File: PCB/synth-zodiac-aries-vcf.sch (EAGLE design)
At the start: 75 parts, among them J4 6.35MM JACK, Q2 PMP4201, Q3 PMP4201, Q4 PMP4201, Q5 PMP4201, Q6 PMP4201, Q7 BC847BPN, Q8 PNP, U2 LM13700, U6 NE5532A

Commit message: Snapshot of designs so far.
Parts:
- removed AUD_OUT, TP1, TP17: TPTHD-038, con-testpoints:TPTHD-038
- removed C22, C23, C24, C25, C27, C29, C30, C34, C35: 0.1uF, rlc:CAPACITOR0603
- removed C26: 100uF/25V, rlc:CAPACITOR_POL-ALUM-SMT-6.3
- removed C28, C31, C32: 2.2uF, rlc:CAPACITOR0603
- removed C33: 2.2uF/16V, rlc:CAPACITOR_POL-ALUM-SMT-4
- removed GND_VCA: TPTHD-SCOPE-LOOP, con-testpoints:TPTHD-SCOPE-LOOP
- removed J4: 6.35MM JACK, con-trs:TRS-JACK-STEREOTE-CK-6.35-29B
- removed JMP1, JMP3, JMP4, JMP5, JMP6, JMP7: NP, rlc:RESISTOR0603
- removed JMP57, JMP58, JMP62: 0, rlc:RESISTOR0603
- removed Q8: PNP, transistor-bjt:PNP-BC856
- removed R26, R29, R32, R34: 1.0K, rlc:RESISTOR0603
- removed R30, R31: 2.74K, rlc:RESISTOR0603
- removed R33, R44, R51: 12.1K, rlc:RESISTOR0603
- removed R35, R41: 68.1K, rlc:RESISTOR0603
- removed R36, R47: 33.2K, rlc:RESISTOR0603
- removed R37: 100K, rlc:RESISTOR0603
- removed R38: 47.5K, rlc:RESISTOR0603
- removed R39, R40, R49: 4.99K, rlc:RESISTOR0603
- removed R42: 100, rlc:RESISTOR0603
- removed R43: 6.81K, rlc:RESISTOR0603
- removed R46, R48: 681R, rlc:RESISTOR0603
- removed R50, R54, R55: 10.0K, rlc:RESISTOR0603
- removed R52: 475R, rlc:RESISTOR0603
- removed R53: 4.75M, rlc:RESISTOR0603
- removed R56: 499K, rlc:RESISTOR0603
- removed U2: LM13700, op-amp:DUAL-BIASLM13700-SMD
- removed VR3, VR4: 10K, rlc:POTRK09?113
- removed VR7: 10K, rlc:TRIMPOTTC33X
- added C1, C8, C9: 2.2uF, rlc:CAPACITOR0603
- added C10, C11, C2, C3, C4, C5, C7: 0.1uF, rlc:CAPACITOR0603
- added C6: 100uF/25V, rlc:CAPACITOR_POL-ALUM-SMT-6.3
- added CAL: 10K, rlc:TRIMPOTTC33X
- added CONST: Aries, circuit-monkey-zodiac:CONSTELLATION-ARIES
- added CUTOFF, RES: 10K, rlc:TRIMPOT9MM_PCB_SHAFT
- added CV_VCF, CV_VCF_MOD, MOD_MIX, TP_VCF_OUT: TPSMD-040-RND, con-testpoints:TPSMD-040-RND
- added GLYPH: Aries, circuit-monkey-zodiac:GLYPH-ARIES
- added J1: (no value), con-jst:04P-VT-SMT
- added MOD_IN, VCF_MOD: 2-pin, VT, SMT, con-jst:02PVT-SMT
- added PCB: PCB FAB, circuit-monkey-zodiac:PENTAGON-40R
- added R1, R7: 68.1K, rlc:RESISTOR0603
- added R10, R11, R12, R13, R15, R16, R18, R8: 1.0K, rlc:RESISTOR0603
- added R14, R9: 2.74K, rlc:RESISTOR0603
- added R17: 12.1K, rlc:RESISTOR0603
- added R2: 47.5K, rlc:RESISTOR0603
- added R4: 33.2K, rlc:RESISTOR0603
- added R5, R6: 4.99K, rlc:RESISTOR0603
- added SHORT1: NP, rlc:SHORT0603
- JMP2: value NP -> 0
- R19: value 100K -> 100
- R20: value 1.0K -> 6.81K
- R21: value 1.0K -> 12.1K
- R22, R3: value 1.0K -> 100K
- VCF_OUT: value TPTHD-038 -> 2-pin, VT, SMT; device con-testpoints:TPTHD-038 -> con-jst:02PVT-SMT
- renumbered R45 to R19
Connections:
- removed net AUDIO_OUT: AUD_OUT.P$1, J4.T, R52.2
- removed net EXP_VCA_CV: R55.1, R56.2
- removed net N$44: C28.2, Q6-A.BASE, R3.2
- removed net N$45: R46.2, U2-B.-
- removed net N$50: Q7P.BASE, R34.2, R35.2, R36.2, R37.2, R38.2, TP17.P$1
- removed net N$51: R35.1, VR7.2
- removed net N$54: R37.1, VR3POT.2
- removed net N$60: R47.2, R48.2, U2-B.+
- removed net N$61: TP1.P$1, U2-B.DIODE-BIAS
- removed net N$62: R49.2, U2-B-BUFFER.IN, U2-B.OUT
- removed net N$63: R50.2, U2-B.AMP-BIAS
- removed net N$64: C33.P, R51.2, U2-B-BUFFER.OUT
- removed net N$65: C33.N, R52.1
- removed net N$66: Q8.COLLECTOR, R50.1, R53.2
- removed net N$67: JMP62.2, Q8.EMITTER
- removed net N$68: JMP62.1, R54.2, R55.2
- removed net N$69: JMP1.2, U2-A.-
- removed net N$70: JMP3.2, U2-A.+
- removed net N$71: JMP5.1, U2-A.OUT
- removed net N$72: JMP2.2, U2-A.DIODE-BIAS
- removed net N$73: JMP4.2, U2-A.AMP-BIAS
- removed net N$74: JMP6.2, U2-A-BUFFER.IN
- removed net N$75: JMP7.1, U2-A-BUFFER.OUT
- removed net VCA_CV: R54.1
- new net CAL: CAL.2, R7.1
- new net CUTOFF: CUTOFF.2, R3.1
- new net MOD_MIX: MOD_MIX.P$1, Q7P.BASE, R2.2, R3.2, R4.2, R7.2, R8.2
- new net VCO_MIX: C1.2, Q6-A.BASE, R15.2
- net +9V: now also C10.2, CUTOFF.3, J1.1, R17.2, R9.2, U6-PWR.V+; no longer C29.2, C34.2, R30.2, R33.2, U2-PWR.VDD, U6-PWR.VDD, VR3POT.3
- net -9V: now also C11.1, CUTOFF.1, J1.2, R6.1, U6-PWR.V-; no longer C30.1, C35.1, R39.1, R53.1, R56.1, U2-PWR.GND, U6-PWR.GND, VR3POT.1
- net EXP_VCF_CV: now also CV_VCF_MOD.P$1, R2.1; no longer R38.1
- net FILT(+): now also C2.2; no longer C22.2
- net FILT(-): now also C2.1; no longer C22.1
- net GND: now also C10.1, C11.2, C6.N, C7.2, J1.4, MOD_IN.2, PCB.GND@1, R14.1, R22.1, R5.2, R8.1, RES.1, VCF_MOD.2, VCF_OUT.2; no longer C26.N, C27.2, C29.1, C30.2, C34.1, C35.2, GND_VCA.P$1, J4.S, Q8.BASE, R19.1, R31.1, R34.1, R40.2, R46.1, R48.1, R49.1, R51.1, VR3-MNT.GND@MT1, VR3-MNT.GND@MT2, VR4-MNT.GND@MT1, VR4-MNT.GND@MT2, VR4POT.1
- net N$32: now also R19.2, R20.1; no longer R42.2, R43.1
- net N$33: now also C8.2, JMP2.1, R22.2; no longer C31.2, JMP58.1, R19.2
- net N$34: now also R10.2, R9.1; no longer R21.2, R30.1
- net N$35: now also C3.1; no longer C23.1
- net N$36: now also C3.2; no longer C23.2
- net N$37: now also R10.1, R11.2; no longer R21.1, R22.2
- net N$38: now also C4.1; no longer C24.1
- net N$39: now also C4.2; no longer C24.2
- net N$40: now also R11.1, R12.2; no longer R22.1, R26.2
- net N$41: now also C5.1; no longer C25.1
- net N$42: now also C5.2; no longer C25.2
- net N$43: now also R12.1, R13.2; no longer R26.1, R29.2
- net N$46: now also R18.2; no longer R32.2
- net N$47: now also R18.1; no longer R32.1
- net N$48: now also C6.P, R13.1, R14.2, R15.1, R16.1; no longer C26.P, R20.1, R29.1, R3.1, R31.2
- net N$49: now also C7.1, R17.1; no longer C27.1, R33.1
- net N$52: now also CAL.3, R6.2; no longer R39.2, VR7.3
- net N$53: now also CAL.1, R5.1; no longer R40.1, VR7.1
- net N$55: now also C1.1, R1.2; no longer C28.1, R41.2
- net N$56: now also R19.1; no longer R42.1
- net N$57: now also C8.1, R20.2, R21.2; no longer C31.1, R43.2, R44.2
- net N$58: now also R21.1, RES.3; no longer R44.1, VR4POT.3
- net N$59: now also C9.2, RES.2; no longer C32.2, VR4POT.2
- net RES_INPUT: now also C9.1, R16.2; no longer C32.1, R20.2
- net VCF_IN: now also CV_VCF.P$1, R1.1, SHORT1.2; no longer JMP57.2, R41.1
- net VCF_MOD: now also R4.1, VCF_MOD.1; no longer R36.1
- net VCF_OUT: now also JMP2.2, TP_VCF_OUT.P$1, VCF_OUT.1; no longer JMP58.2, R47.1, VCF_OUT.P$1
- net VCO_OUT: now also MOD_IN.1, SHORT1.1; no longer JMP57.1
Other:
- note added: "2.6V"
- note added: "3.55V"
- note added: "4.5V"
- note added: "5.45V"
- note added: "6.4V"
- note added: "===> VCA"
- note added: "CV Panel ===>"
- note added: "NC"
- note added: "VCF MOD ===>"
- note added: "VCO / CV Panel ===>"
- note removed: "10.6V"
- note removed: "4.3V"
- note removed: "5.8V"
- note removed: "7.4V"
- note removed: "9.4V"
- note removed: "VCA"
- moved on the sheet: JMP2, Q2-A, Q2-B, Q3-A, Q3-B, Q4-A, Q4-B, Q5-A, Q5-B, Q6-A, Q6-B, Q7N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

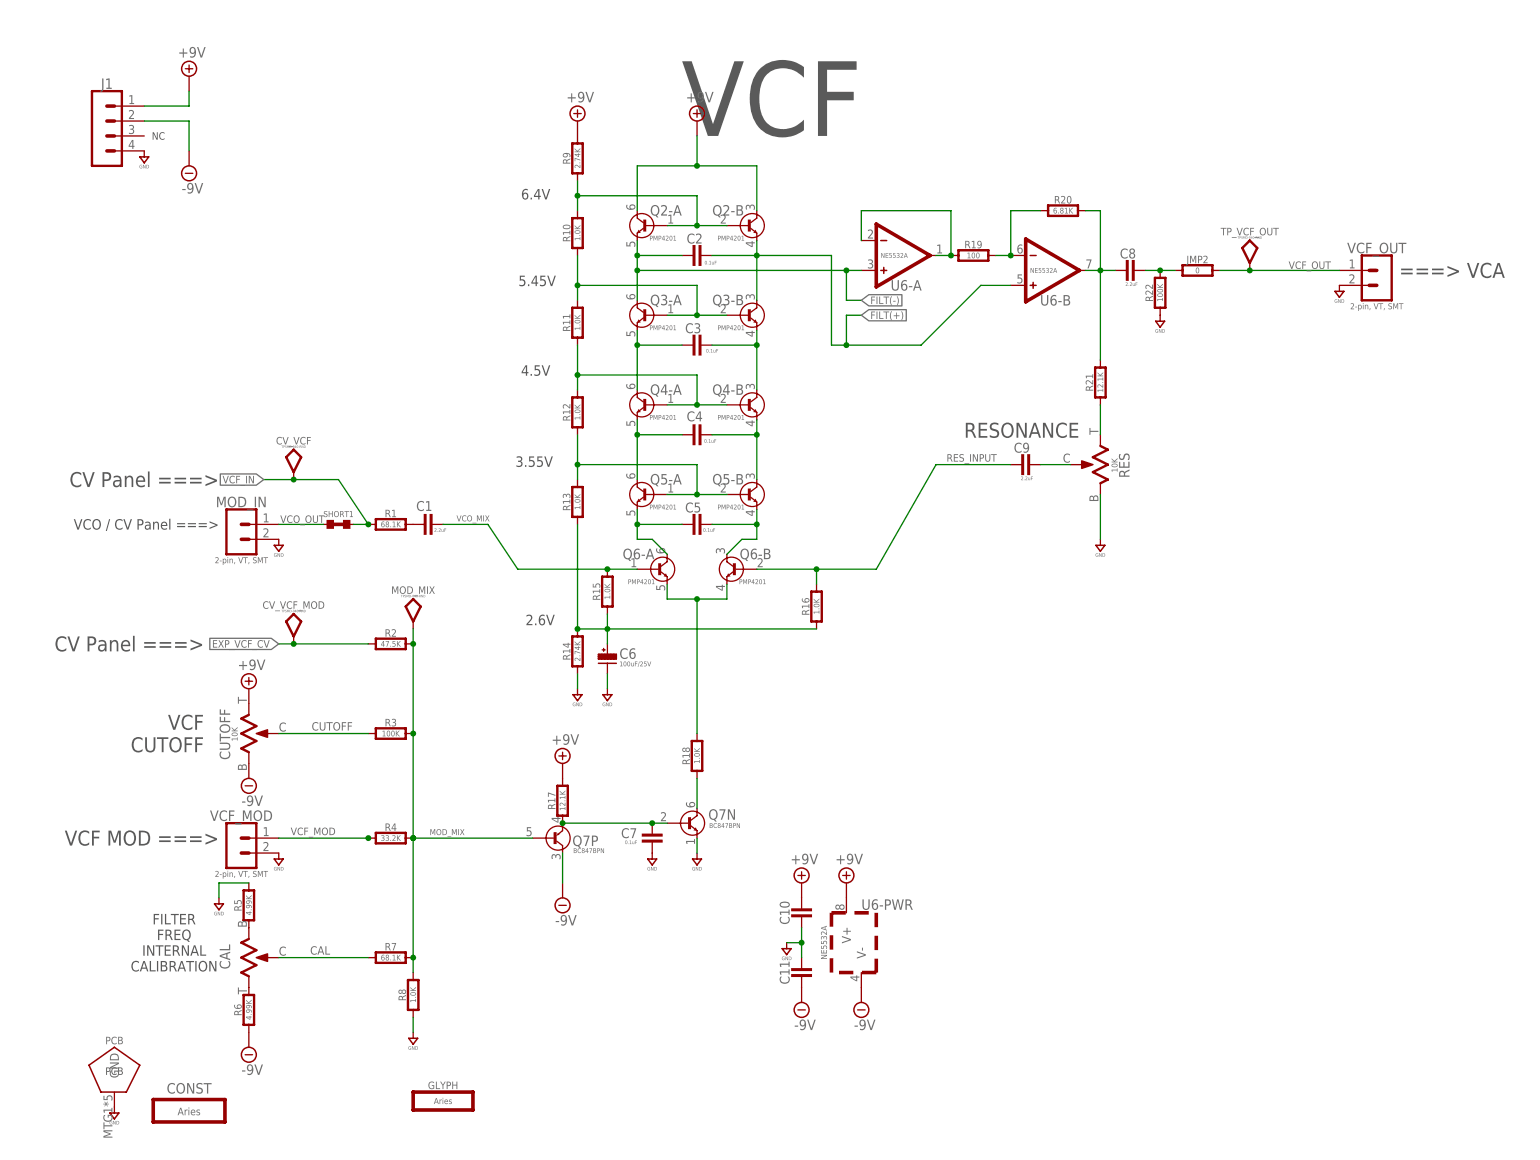
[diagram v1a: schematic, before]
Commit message: Almost ready for FAB.
Sagittarius was mis-spelled, renamed it.  Taurus is still WIP.
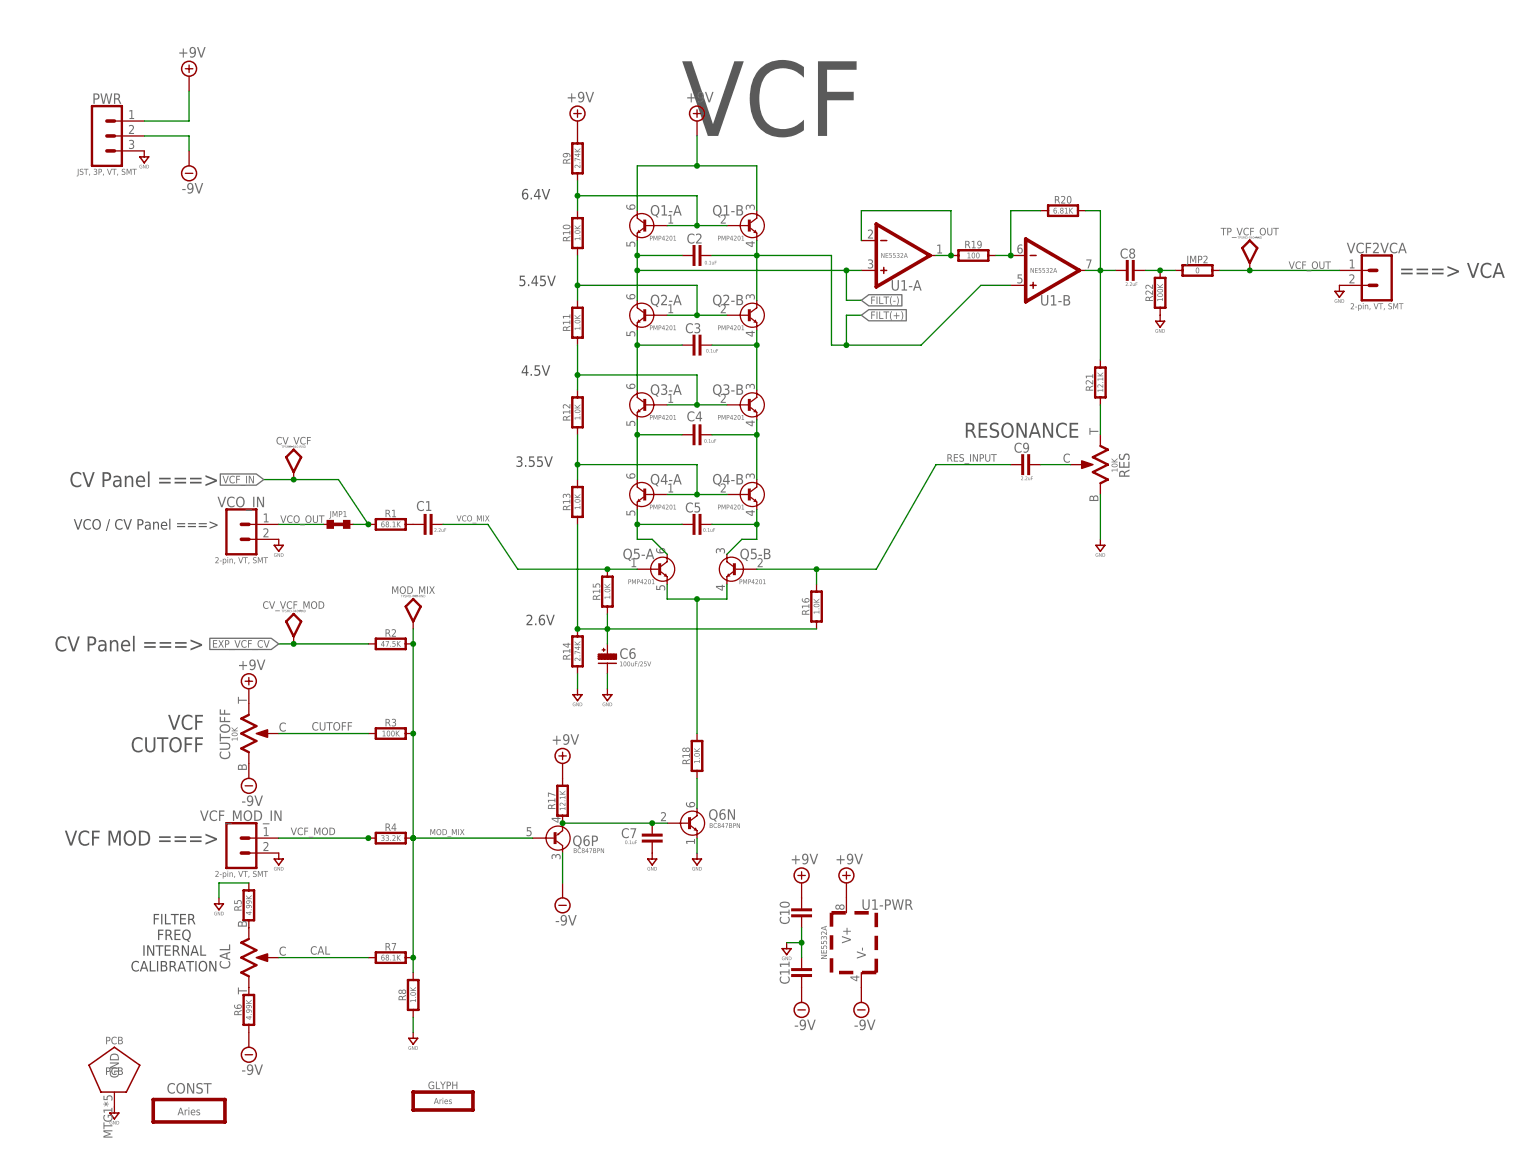
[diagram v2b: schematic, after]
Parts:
- removed J1: (no value), con-jst:04P-VT-SMT
- removed Q7: BC847BPN, transistor-bjt:NPN-PNPBC847BPN
- added PWR: JST, 3P, VT, SMT, con-jst:03P-VT-SMT
- added Q1: PMP4201, transistor-bjt:NPN-DUALPMP4201
- Q6: value PMP4201 -> BC847BPN; device transistor-bjt:NPN-DUALPMP4201 -> transistor-bjt:NPN-PNPBC847BPN
- renumbered MOD_IN to VCO_IN, SHORT1 to JMP1, U6 to U1, VCF_MOD to VCF_MOD_IN, VCF_OUT to VCF2VCA
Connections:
- net +9V: now also PWR.1, Q1-A.COLLECTOR, Q1-B.COLLECTOR; no longer J1.1, Q2-A.COLLECTOR, Q2-B.COLLECTOR
- net -9V: now also PWR.2, Q6P.COLLECTOR; no longer J1.2, Q7P.COLLECTOR
- net FILT(+): now also Q1-B.EMITTER, Q2-B.COLLECTOR; no longer Q2-B.EMITTER, Q3-B.COLLECTOR
- net FILT(-): now also Q1-A.EMITTER, Q2-A.COLLECTOR; no longer Q2-A.EMITTER, Q3-A.COLLECTOR
- net GND: now also PWR.3, Q6N.EMITTER; no longer J1.4, Q7N.EMITTER
- net MOD_MIX: now also Q6P.BASE; no longer Q7P.BASE
- net N$34: now also Q1-A.BASE, Q1-B.BASE; no longer Q2-A.BASE, Q2-B.BASE
- net N$35: now also Q2-A.EMITTER, Q3-A.COLLECTOR; no longer Q3-A.EMITTER, Q4-A.COLLECTOR
- net N$36: now also Q2-B.EMITTER, Q3-B.COLLECTOR; no longer Q3-B.EMITTER, Q4-B.COLLECTOR
- net N$37: now also Q2-A.BASE, Q2-B.BASE; no longer Q3-A.BASE, Q3-B.BASE
- net N$38: now also Q3-A.EMITTER, Q4-A.COLLECTOR; no longer Q4-A.EMITTER, Q5-A.COLLECTOR
- net N$39: now also Q3-B.EMITTER, Q4-B.COLLECTOR; no longer Q4-B.EMITTER, Q5-B.COLLECTOR
- net N$40: now also Q3-A.BASE, Q3-B.BASE; no longer Q4-A.BASE, Q4-B.BASE
- net N$41: now also Q4-A.EMITTER, Q5-A.COLLECTOR; no longer Q5-A.EMITTER, Q6-A.COLLECTOR
- net N$42: now also Q4-B.EMITTER, Q5-B.COLLECTOR; no longer Q5-B.EMITTER, Q6-B.COLLECTOR
- net N$43: now also Q4-A.BASE, Q4-B.BASE; no longer Q5-A.BASE, Q5-B.BASE
- net N$46: now also Q5-A.EMITTER, Q5-B.EMITTER; no longer Q6-A.EMITTER, Q6-B.EMITTER
- net N$47: now also Q6N.COLLECTOR; no longer Q7N.COLLECTOR
- net N$49: now also Q6N.BASE, Q6P.EMITTER; no longer Q7N.BASE, Q7P.EMITTER
- net RES_INPUT: now also Q5-B.BASE; no longer Q6-B.BASE
- net VCO_MIX: now also Q5-A.BASE; no longer Q6-A.BASE
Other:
- note removed: "NC"
- moved on the sheet: Q2-A, Q2-B, Q3-A, Q3-B, Q4-A, Q4-B, Q5-A, Q5-B

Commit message: Work in progress for rev A,  VCO rev.B
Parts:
- removed CV_VCF_MOD: TPSMD-040-RND, con-testpoints:TPSMD-040-RND
- removed JMP2: 0, rlc:RESISTOR0603
- added C_0-5, C_GND: PADSMD-070X070, con-testpoints:PADSMD-070X070
- added R23: 150K, rlc:RESISTOR0603
- added R24: 47K, rlc:RESISTOR0603
- PWR: value JST, 3P, VT, SMT -> JST SM 3P; device con-jst:03P-VT-SMT -> con-jst:03P-SM-VT-SMT
- R2: value 47.5K -> 150K
- VCF2VCA, VCF_MOD_IN, VCO_IN: value 2-pin, VT, SMT -> JST, SH, 2P; device con-jst:02PVT-SMT -> con-jst:02P-SM-VT-SMT
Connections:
- net VCO_OUT renamed FROM_VCO
- removed net EXP_VCF_CV: CV_VCF_MOD.P$1, R2.1
- removed net N$33: C8.2, JMP2.1, R22.2
- new net CUT_5: C_0-5.PAD, R2.1, R23.2, R24.2
- net +9V: now also R2.2
- net CUTOFF: now also R23.1
- net GND: now also C_GND.PAD, R24.1
- net MOD_MIX: no longer R2.2
- net VCF_OUT: now also C8.2, R22.2; no longer JMP2.2
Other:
- note added: "Aries"
- note added: "Convert -9 to +9 range to 0-3.3V for LED PCB."
- note added: "From VCO ===>"
- note added: "SATAN'S CYCLE WORKS"
- note added: "TO LED BOARD"
- note added: "Zodiac Synth"
- note removed: "CV Panel ===>"
- note removed: "VCO / CV Panel ===>"
- moved on the sheet: C1, C10, C11, C2, C3, C4, C5, C6, C7, C8, C9, CAL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

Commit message: Tune values and some schematic visual tweaks.
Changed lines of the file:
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@@
 <instance part="CAL" gate="G$1" x="30.48" y="20.32" smashed="yes" rot="MR270">
 <attribute name="NAME" x="26.416" y="20.447" size="1.778" layer="95" ratio="15" rot="MR270" align="center"/>
+<attribute name="VALUE" x="28.067" y="20.447" size="1.016" layer="96" rot="MR270" align="center"/>
 </instance>
 <instance part="R6" gate="G$1" x="30.48" y="10.16" smashed="yes" rot="R90">
@@
 </instance>
 <instance part="C10" gate="G$1" x="165.1" y="45.72" smashed="yes" rot="R180">
-<attribute name="NAME" x="163.068" y="43.688" size="1.6764" layer="95" font="vector" ratio="15" rot="R90"/>
+<attribute name="NAME" x="162.56" y="45.72" size="1.6764" layer="95" font="vector" ratio="15" rot="R180"/>
+<attribute name="VALUE" x="162.56" y="46.736" size="0.6096" layer="96" font="vector" rot="R180"/>
 </instance>
 <instance part="C11" gate="G$1" x="165.1" y="35.56" smashed="yes" rot="R180">
-<attribute name="NAME" x="163.068" y="33.528" size="1.6764" layer="95" font="vector" ratio="15" rot="R90"/>
+<attribute name="NAME" x="162.56" y="35.56" size="1.6764" layer="95" font="vector" ratio="15" rot="R180"/>
+<attribute name="VALUE" x="162.56" y="36.576" size="0.6096" layer="96" font="vector" rot="R180"/>
 </instance>
 <instance part="SUPPLY45" gate="GND" x="162.56" y="40.64" smashed="yes">
